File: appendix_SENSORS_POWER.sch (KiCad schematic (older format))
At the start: 53 parts, among them J401 Conn_01x02, J402 Conn_01x02, J403 Screw_Terminal_01x02, J404 Conn_01x02, J405 Conn_01x02, J406 Screw_Terminal_01x02, J407 Conn_01x02, J408 Conn_01x02, J409 Conn_01x02, J410 Conn_01x02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

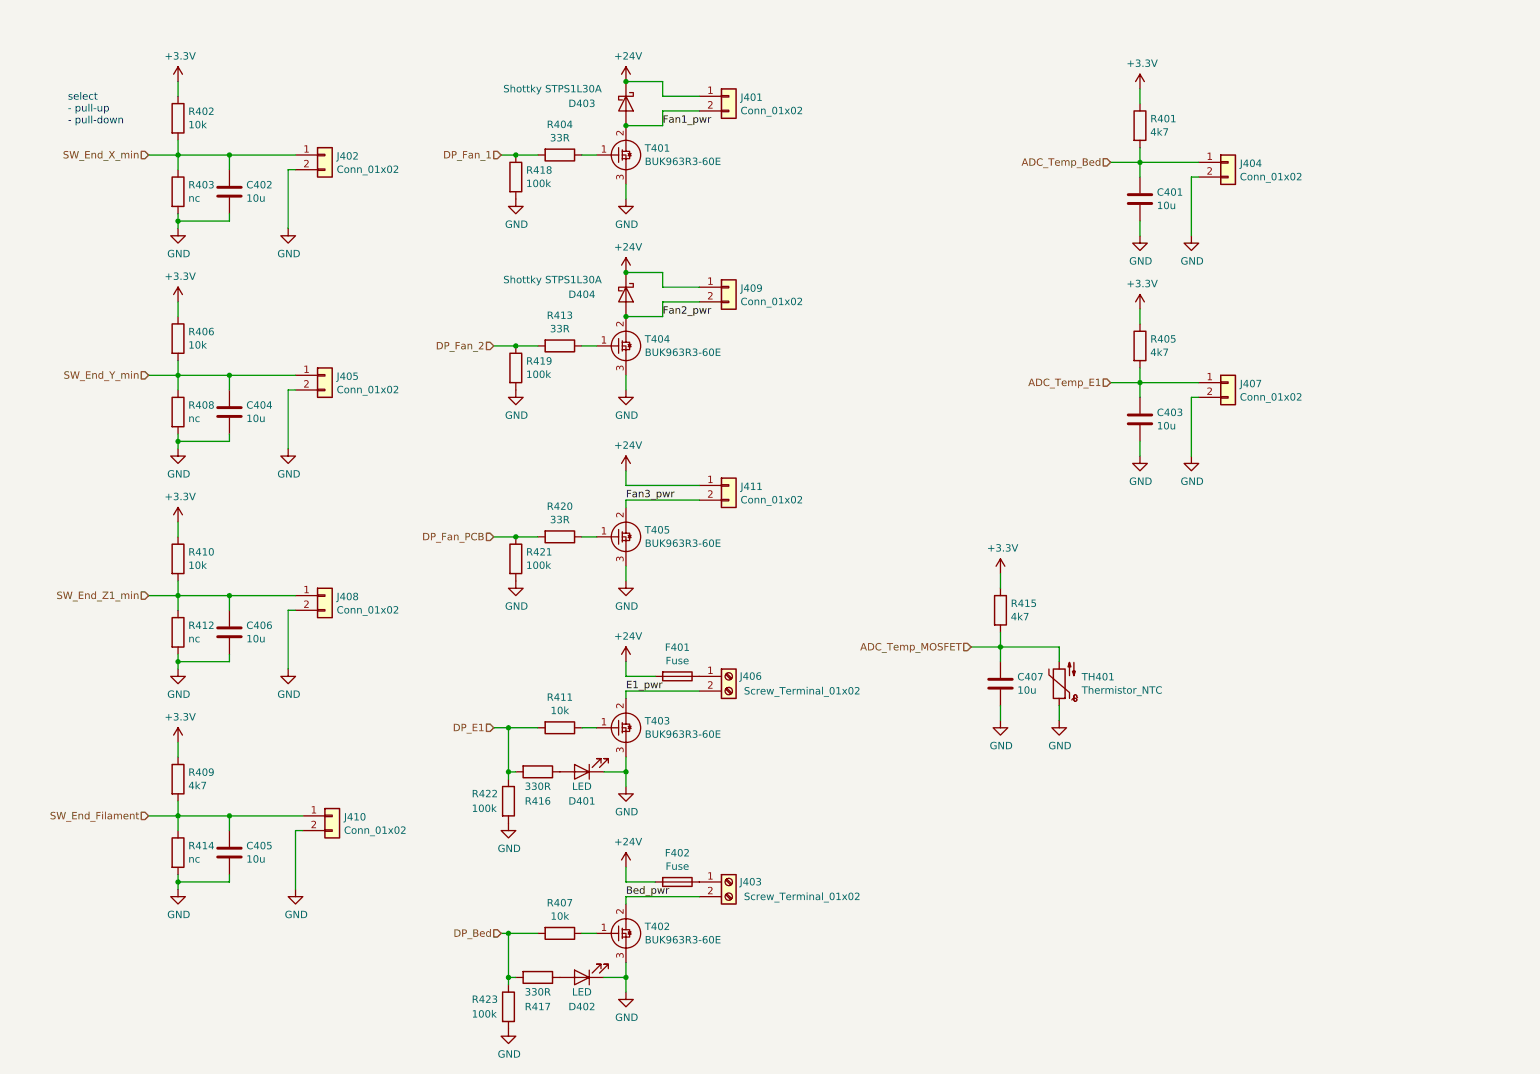
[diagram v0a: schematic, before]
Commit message: started with STM32 Pinout connections (Mittagspause)
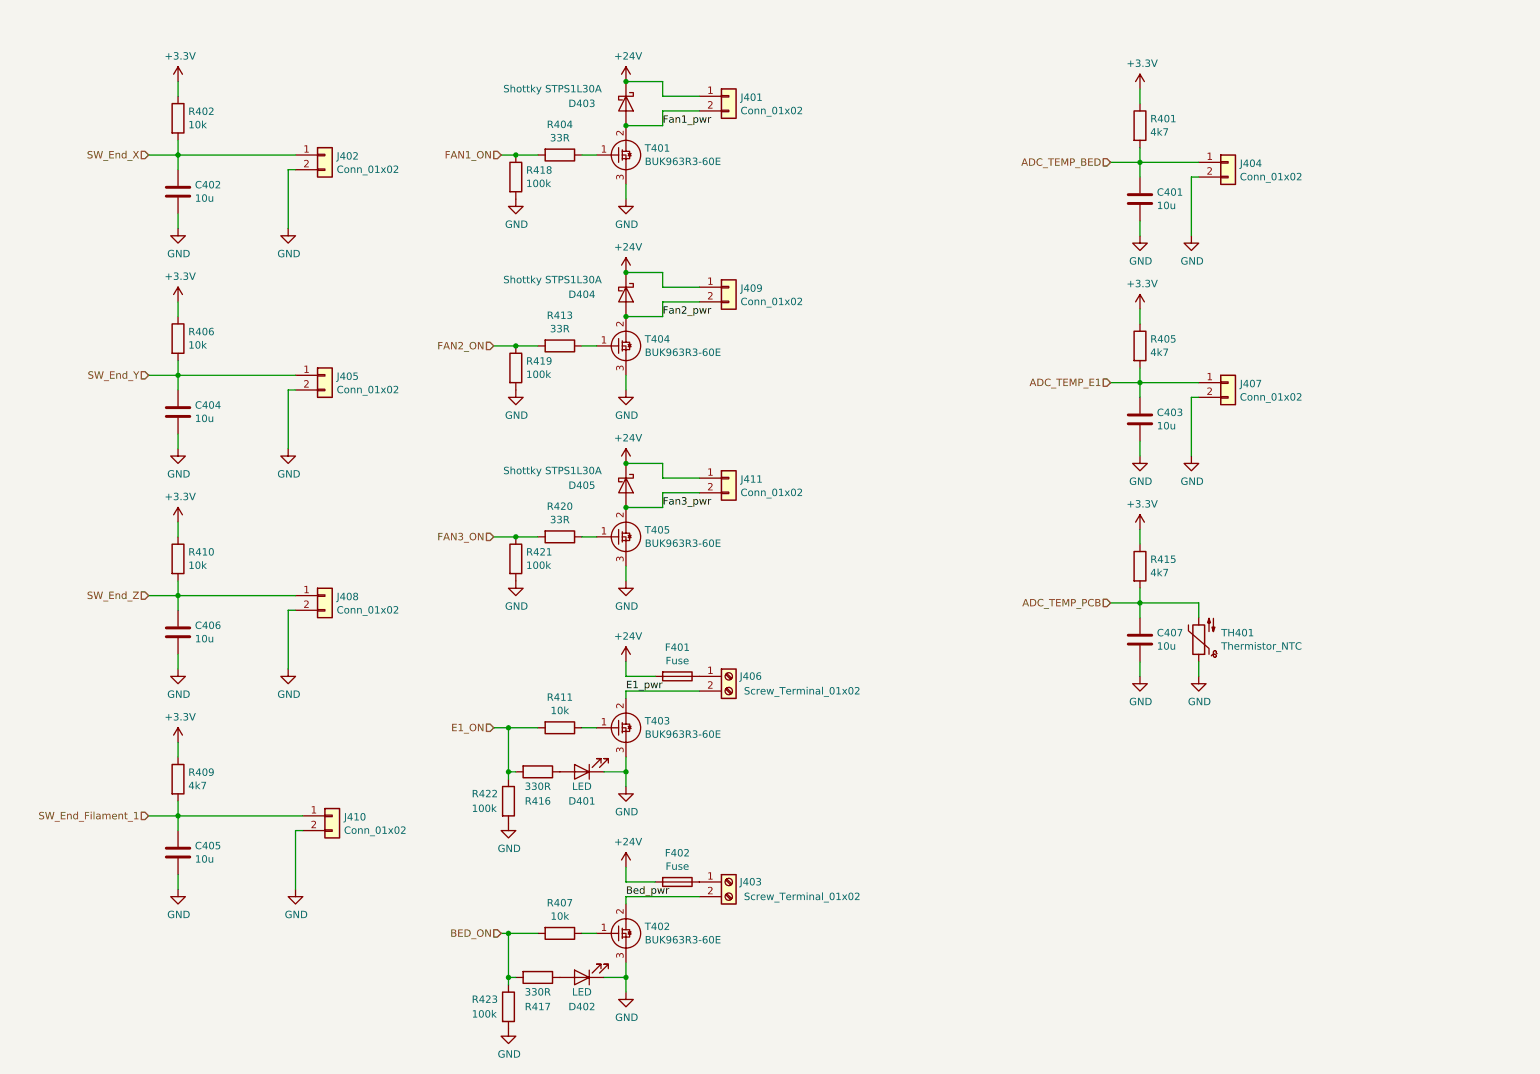
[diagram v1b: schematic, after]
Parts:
- removed R403, R408, R412, R414: nc, Resistors_SMD:R_0603, symbol Device:R
- added D405: Shottky STPS1L30A, Diodes_SMD:D_SMB, symbol Device:D_Schottky
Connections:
- net +24V: now also D405.1 (K)
- net Fan3_pwr: now also D405.2 (A)
- net ADC_Temp_Bed renamed ADC_TEMP_BED
- net ADC_Temp_E1 renamed ADC_TEMP_E1
- net ADC_Temp_MOSFET renamed ADC_TEMP_PCB
- net DP_Bed renamed BED_ON
- net DP_E1 renamed E1_ON
- net DP_Fan_1 renamed FAN1_ON
- net DP_Fan_2 renamed FAN2_ON
- net DP_Fan_PCB renamed FAN3_ON
- net SW_End_Filament renamed SW_End_Filament_1
- net SW_End_X_min renamed SW_End_X
- net SW_End_Y_min renamed SW_End_Y
- net SW_End_Z1_min renamed SW_End_Z
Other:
- note removed: "select\n- pull-up\n- pull-down"
- moved on the sheet: C402, C404, C405, C406, C407, J411, R415, TH401

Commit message: cleaned up Layout
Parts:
- removed T401, T404, T405: BUK963R3-60E, Package_TO_SOT_SMD:TO-263-2, symbol FHNW-Pro4E-FS19T8-Library:BUK963R3-60E
- added T401, T404, T405: PMV40UN2, Package_TO_SOT_SMD:SOT-23, symbol Transistor_FET:2N7002
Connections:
- net Fan1_pwr: now also T401.3 (D)
- net Fan2_pwr: now also T404.3 (D)
- net Fan3_pwr: now also T405.3 (D)
- net GND: now also T401.2 (S), T404.2 (S), T405.2 (S)
- net at R420.1: now also T405.1 (G)
- net at R404.1: now also T401.1 (G)
- net at R413.1: now also T404.1 (G)
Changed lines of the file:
@@
 	1700 1550 1700 1450
-$Comp
-L FHNW-Pro4E-FS19T8-Library:BUK963R3-60E T401
-U 1 1 5CCB900F
-P 4750 1550
-F 0 "T401" H 4878 1596 50  0000 L CNN
-F 1 "BUK963R3-60E" H 4878 1505 50  0000 L CNN
-F 2 "Package_TO_SOT_SMD:TO-263-2" H 5550 1150 50  0001 C CNN
-F 3 "http://www.farnell.com/datasheets/2174111.pdf?_ga=2.163468607.22968134.1552994068-1575888051.1538557827" H 4750 1000 50  0001 C CNN
-	1    4750 1550
-	1    0    0    -1
-$EndComp
 $Comp
 L power:GND #PWR0142
@@
 	0    1    1    0
 $EndComp
-Wire Wire Line
-	4450 1550 4550 1550
 $Comp
 L FHNW-Pro4E-FS19T8-Library:BUK963R3-60E T402
@@
 $EndComp
 $Comp
-L FHNW-Pro4E-FS19T8-Library:BUK963R3-60E T404
-U 1 1 5CDE31B1
-P 4750 2850
-F 0 "T404" H 4878 2896 50  0000 L CNN
-F 1 "BUK963R3-60E" H 4878 2805 50  0000 L CNN
-F 2 "Package_TO_SOT_SMD:TO-263-2" H 5550 2450 50  0001 C CNN
-F 3 "http://www.farnell.com/datasheets/2174111.pdf?_ga=2.163468607.22968134.1552994068-1575888051.1538557827" H 4750 2300 50  0001 C CNN
-	1    4750 2850
-	1    0    0    -1
-$EndComp
-$Comp
 L Device:R R413
 U 1 1 5CDE31C6
@@
 	0    1    1    0
 $EndComp
-Wire Wire Line
-	4450 2850 4550 2850
 $Comp
 L Connector:Screw_Terminal_01x02 J?
@@
 	4750 3150 4750 3050
 $Comp
-L FHNW-Pro4E-FS19T8-Library:BUK963R3-60E T405
-U 1 1 5CBD0C42
-P 4750 4150
-F 0 "T405" H 4878 4196 50  0000 L CNN
-F 1 "BUK963R3-60E" H 4878 4105 50  0000 L CNN
-F 2 "Package_TO_SOT_SMD:TO-263-2" H 5550 3750 50  0001 C CNN
-F 3 "http://www.farnell.com/datasheets/2174111.pdf?_ga=2.163468607.22968134.1552994068-1575888051.1538557827" H 4750 3600 50  0001 C CNN
-	1    4750 4150
-	1    0    0    -1
-$EndComp
-$Comp
 L Device:R R420
 U 1 1 5CBD0C4C
@@
 	0    1    1    0
 $EndComp
-Wire Wire Line
-	4450 4150 4550 4150
 $Comp
 L Connector_Generic:Conn_01x02 J411
@@
 Wire Wire Line
 	5000 1350 5000 1250
-Connection ~ 4750 1350
 Wire Wire Line
 	5000 1150 5250 1150
@@
 Wire Wire Line
 	5000 2650 4750 2650
-Connection ~ 4750 2650
 Wire Wire Line
 	1700 1550 2500 1550
@@
 Wire Wire Line
 	4750 3950 5000 3950
-Connection ~ 4750 3950
 Wire Wire Line
 	5250 3750 5000 3750
@@
 Text HLabel 8050 1600 0    50   Input ~ 0
 ADC_TEMP_BED
+Connection ~ 4750 1350
+$Comp
+L Transistor_FET:2N7002 T401
+U 1 1 5CBEA1BD
+P 4650 1550
+F 0 "T401" H 4856 1596 50  0000 L CNN
+F 1 "PMV40UN2" H 4856 1505 50  0000 L CNN
+F 2 "Package_TO_SOT_SMD:SOT-23" H 4850 1475 50  0001 L CIN
+F 3 "https://www.fairchildsemi.com/datasheets/2N/2N7002.pdf" H 4650 1550 50  0001 L CNN
+	1    4650 1550
+	1    0    0    -1
+$EndComp
+$Comp
+L Transistor_FET:2N7002 T404
+U 1 1 5CBFF7F5
+P 4650 2850
+F 0 "T404" H 4856 2896 50  0000 L CNN
+F 1 "PMV40UN2" H 4856 2805 50  0000 L CNN
+F 2 "Package_TO_SOT_SMD:SOT-23" H 4850 2775 50  0001 L CIN
+F 3 "https://www.fairchildsemi.com/datasheets/2N/2N7002.pdf" H 4650 2850 50  0001 L CNN
+	1    4650 2850
+	1    0    0    -1
+$EndComp
+$Comp
+L Transistor_FET:2N7002 T405
+U 1 1 5CC0134D
+P 4650 4150
+F 0 "T405" H 4856 4196 50  0000 L CNN
+F 1 "PMV40UN2" H 4856 4105 50  0000 L CNN
+F 2 "Package_TO_SOT_SMD:SOT-23" H 4850 4075 50  0001 L CIN
+F 3 "https://www.fairchildsemi.com/datasheets/2N/2N7002.pdf" H 4650 4150 50  0001 L CNN
+	1    4650 4150
+	1    0    0    -1
+$EndComp
+Connection ~ 4750 3950
+Connection ~ 4750 2650
 $EndSCHEMATC

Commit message: having issues with netclasses
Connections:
- net +3V3: no longer R401.1, R405.1, R415.1
- net BED_ON renamed BED_SIG_ON
- net E1_ON renamed E1_SIG_ON
- new net +3.3VA: R401.1, R405.1, R415.1
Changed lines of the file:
@@
 $Descr A4 11693 8268
 encoding utf-8
-Sheet 4 6
+Sheet 6 6
 Title ""
 Date ""
@@
 	1    0    0    -1
 $EndComp
-$Comp
-L power:+3.3V #PWR0140
-U 1 1 5CA3C033
-P 1700 1050
-F 0 "#PWR0140" H 1700 900 50  0001 C CNN
-F 1 "+3.3V" H 1715 1223 50  0000 C CNN
-F 2 "" H 1700 1050 50  0001 C CNN
-F 3 "" H 1700 1050 50  0001 C CNN
-	1    1700 1050
-	1    0    0    -1
-$EndComp
 Wire Wire Line
 	1700 1050 1700 1150
@@
 	1700 5550 1700 5650
 $Comp
-L power:+3.3V #PWR0147
-U 1 1 5CA3A806
-P 1700 5550
-F 0 "#PWR0147" H 1700 5400 50  0001 C CNN
-F 1 "+3.3V" H 1715 5723 50  0000 C CNN
-F 2 "" H 1700 5550 50  0001 C CNN
-F 3 "" H 1700 5550 50  0001 C CNN
-	1    1700 5550
-	1    0    0    -1
-$EndComp
-$Comp
 L power:GND #PWR0148
 U 1 1 5CA3A800
@@
 	8250 2600 8250 2700
 $Comp
-L power:+3.3V #PWR0149
-U 1 1 5CA3A64A
-P 8250 2600
-F 0 "#PWR0149" H 8250 2450 50  0001 C CNN
-F 1 "+3.3V" H 8265 2773 50  0000 C CNN
-F 2 "" H 8250 2600 50  0001 C CNN
-F 3 "" H 8250 2600 50  0001 C CNN
-	1    8250 2600
-	1    0    0    -1
-$EndComp
-$Comp
 L power:GND #PWR0150
 U 1 1 5CA3A644
@@
 	8250 1100 8250 1200
 $Comp
-L power:+3.3V #PWR0151
-U 1 1 5CA3A344
-P 8250 1100
-F 0 "#PWR0151" H 8250 950 50  0001 C CNN
-F 1 "+3.3V" H 8265 1273 50  0000 C CNN
-F 2 "" H 8250 1100 50  0001 C CNN
-F 3 "" H 8250 1100 50  0001 C CNN
-	1    8250 1100
-	1    0    0    -1
-$EndComp
-$Comp
 L power:GND #PWR0152
 U 1 1 5CA3A309
@@
 	1    0    0    -1
 $EndComp
-$Comp
-L power:+3.3V #PWR0154
-U 1 1 5CA77FA5
-P 1700 2550
-F 0 "#PWR0154" H 1700 2400 50  0001 C CNN
-F 1 "+3.3V" H 1715 2723 50  0000 C CNN
-F 2 "" H 1700 2550 50  0001 C CNN
-F 3 "" H 1700 2550 50  0001 C CNN
-	1    1700 2550
-	1    0    0    -1
-$EndComp
 Wire Wire Line
 	1700 2550 1700 2650
@@
 F 3 "" H 1700 5050 50  0001 C CNN
 	1    1700 5050
-	1    0    0    -1
-$EndComp
-$Comp
-L power:+3.3V #PWR0156
-U 1 1 5CA7DA0D
-P 1700 4050
-F 0 "#PWR0156" H 1700 3900 50  0001 C CNN
-F 1 "+3.3V" H 1715 4223 50  0000 C CNN
-F 2 "" H 1700 4050 50  0001 C CNN
-F 3 "" H 1700 4050 50  0001 C CNN
-	1    1700 4050
 	1    0    0    -1
 $EndComp
@@
 	8250 4100 8250 4200
 $Comp
-L power:+3.3V #PWR0412
-U 1 1 5CCFF1D0
-P 8250 4100
-F 0 "#PWR0412" H 8250 3950 50  0001 C CNN
-F 1 "+3.3V" H 8265 4273 50  0000 C CNN
-F 2 "" H 8250 4100 50  0001 C CNN
-F 3 "" H 8250 4100 50  0001 C CNN
-	1    8250 4100
-	1    0    0    -1
-$EndComp
-$Comp
 L power:GND #PWR0413
 U 1 1 5CCFF1D6
@@
 FAN3_ON
 Text HLabel 3900 6850 0    50   Input ~ 0
-BED_ON
+BED_SIG_ON
 Text HLabel 3850 5450 0    50   Input ~ 0
-E1_ON
+E1_SIG_ON
 Text HLabel 8050 3100 0    50   Input ~ 0
 ADC_TEMP_E1
@@
 Connection ~ 4750 3950
 Connection ~ 4750 2650
+$Comp
+L power:+3.3V #PWR0147
+U 1 1 5CA3A806
+P 1700 5550
+F 0 "#PWR0147" H 1700 5400 50  0001 C CNN
+F 1 "+3.3V" H 1715 5723 50  0000 C CNN
+F 2 "" H 1700 5550 50  0001 C CNN
+F 3 "" H 1700 5550 50  0001 C CNN
+	1    1700 5550
+	1    0    0    -1
+$EndComp
+$Comp
+L power:+3.3V #PWR0156
+U 1 1 5CA7DA0D
+P 1700 4050
+F 0 "#PWR0156" H 1700 3900 50  0001 C CNN
+F 1 "+3.3V" H 1715 4223 50  0000 C CNN
+F 2 "" H 1700 4050 50  0001 C CNN
+F 3 "" H 1700 4050 50  0001 C CNN
+	1    1700 4050
+	1    0    0    -1
+$EndComp
+$Comp
+L power:+3.3V #PWR0154
+U 1 1 5CA77FA5
+P 1700 2550
+F 0 "#PWR0154" H 1700 2400 50  0001 C CNN
+F 1 "+3.3V" H 1715 2723 50  0000 C CNN
+F 2 "" H 1700 2550 50  0001 C CNN
+F 3 "" H 1700 2550 50  0001 C CNN
+	1    1700 2550
+	1    0    0    -1
+$EndComp
+$Comp
+L power:+3.3V #PWR0140
+U 1 1 5CA3C033
+P 1700 1050
+F 0 "#PWR0140" H 1700 900 50  0001 C CNN
+F 1 "+3.3V" H 1715 1223 50  0000 C CNN
+F 2 "" H 1700 1050 50  0001 C CNN
+F 3 "" H 1700 1050 50  0001 C CNN
+	1    1700 1050
+	1    0    0    -1
+$EndComp
+$Comp
+L power:+3.3VA #PWR?
+U 1 1 5CCEB52C
+P 8250 4100
+AR Path="/5CCEB52C" Ref="#PWR?"  Part="1"
+AR Path="/5CA39F21/5CCEB52C" Ref="#PWR0149"  Part="1"
+F 0 "#PWR0149" H 8250 3950 50  0001 C CNN
+F 1 "+3.3VA" H 8265 4273 50  0000 C CNN
+F 2 "" H 8250 4100 50  0001 C CNN
+F 3 "" H 8250 4100 50  0001 C CNN
+	1    8250 4100
+	1    0    0    -1
+$EndComp
+$Comp
+L power:+3.3VA #PWR?
+U 1 1 5CCEE8E5
+P 8250 2600
+AR Path="/5CCEE8E5" Ref="#PWR?"  Part="1"
+AR Path="/5CA39F21/5CCEE8E5" Ref="#PWR0151"  Part="1"
+F 0 "#PWR0151" H 8250 2450 50  0001 C CNN
+F 1 "+3.3VA" H 8265 2773 50  0000 C CNN
+F 2 "" H 8250 2600 50  0001 C CNN
+F 3 "" H 8250 2600 50  0001 C CNN
+	1    8250 2600
+	1    0    0    -1
+$EndComp
+$Comp
+L power:+3.3VA #PWR?
+U 1 1 5CCF1D5B
+P 8250 1100
+AR Path="/5CCF1D5B" Ref="#PWR?"  Part="1"
+AR Path="/5CA39F21/5CCF1D5B" Ref="#PWR0172"  Part="1"
+F 0 "#PWR0172" H 8250 950 50  0001 C CNN
+F 1 "+3.3VA" H 8265 1273 50  0000 C CNN
+F 2 "" H 8250 1100 50  0001 C CNN
+F 3 "" H 8250 1100 50  0001 C CNN
+	1    8250 1100
+	1    0    0    -1
+$EndComp
 $EndSCHEMATC
